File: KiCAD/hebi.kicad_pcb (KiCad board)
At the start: 4 copper layers, 49 x 49 mm, 99 parts, among them K1 CONN_3, K2 CONN_3, K3 CONN_3, K4 CONN_3, K5 CONN_3, P1 CONN_4, P2 CONN_4, P3 CONN_4, P4 CONN_4, P6 CONN_2, Q1 MOS_N_DIODE, Q10 MOS_N_DIODE, Q2 MOS_N_DIODE, Q3 MOS_N_DIODE, Q4 MOS_N_DIODE, Q5 MOS_N_DIODE, Q6 MOS_N_DIODE, Q7 MOS_N_DIODE, Q9 MOS_N_DIODE, SW1 SW_PUSH, SW2 SW_PUSH, SW3 SW_PUSH, U3 MCP1825S, U4 STM32F407VG, U5 XBEE, X1 8MHz

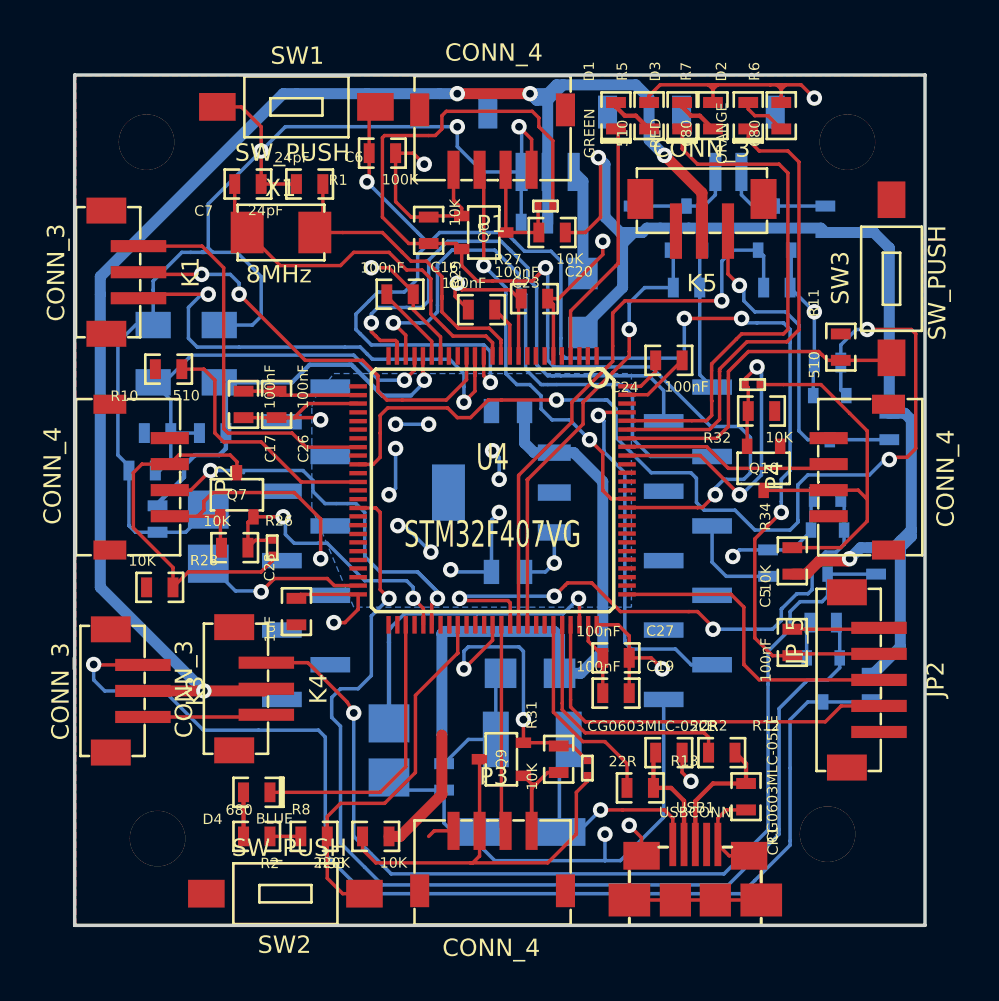
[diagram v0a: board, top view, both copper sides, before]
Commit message: Routed things, power planes added, rounded corners.
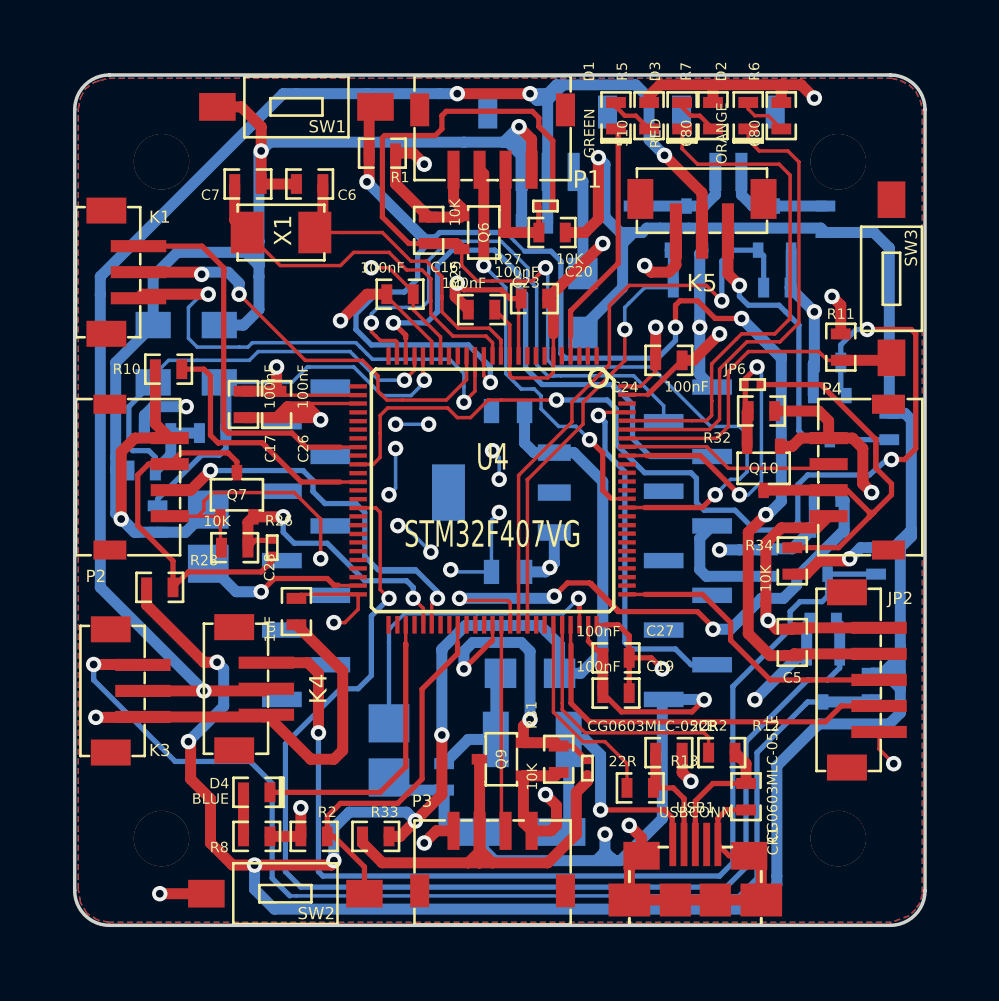
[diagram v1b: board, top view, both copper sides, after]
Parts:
- moved Taladro3mm 1.42 mm to (178.8, 116.7)
- moved Taladro3mm 1.25 mm to (217.8, 116.7)
- moved Taladro3mm 0.67 mm to (217.8, 155.7)
- moved Taladro3mm 0.22 mm to (178.8, 155.7)
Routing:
- net GND: track 218.7 -> 531.4 mm, vias 18 -> 28
- net VCC: track 110.9 -> 338.9 mm, vias 10 -> 18
- net +5V: track 116.3 -> 208.6 mm, vias 2 -> 8
- net /SERVO3_3V: track 58.1 -> 95.7 mm
- net /RESET: track 85.2 -> 122.8 mm
- net /XBEE_RX: track 33.3 -> 62.8 mm
- net /SERVO1_3V: track 64.7 -> 91.6 mm
- net /SERVO1_5V: track 66.5 -> 90.5 mm
- net /ADC3: track 22.9 -> 43.0 mm
- net /TX1_3V: track 61.9 -> 81.6 mm
- net /RX3: track 24.7 -> 43.9 mm
- net /TX3: track 21.4 -> 36.0 mm
- net /SERVO2_5V: track 59.0 -> 72.9 mm
- net /TX2: track 24.0 -> 37.8 mm
- net /LED1: track 14.3 -> 25.9 mm
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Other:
- outline, holes or cut-outs redrawn
- net class Medium added: clearance 0.254, trace_width 0.3048, via_dia 0.889, via_drill 0.635

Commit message: Fixed silkscreen (now it is nice)
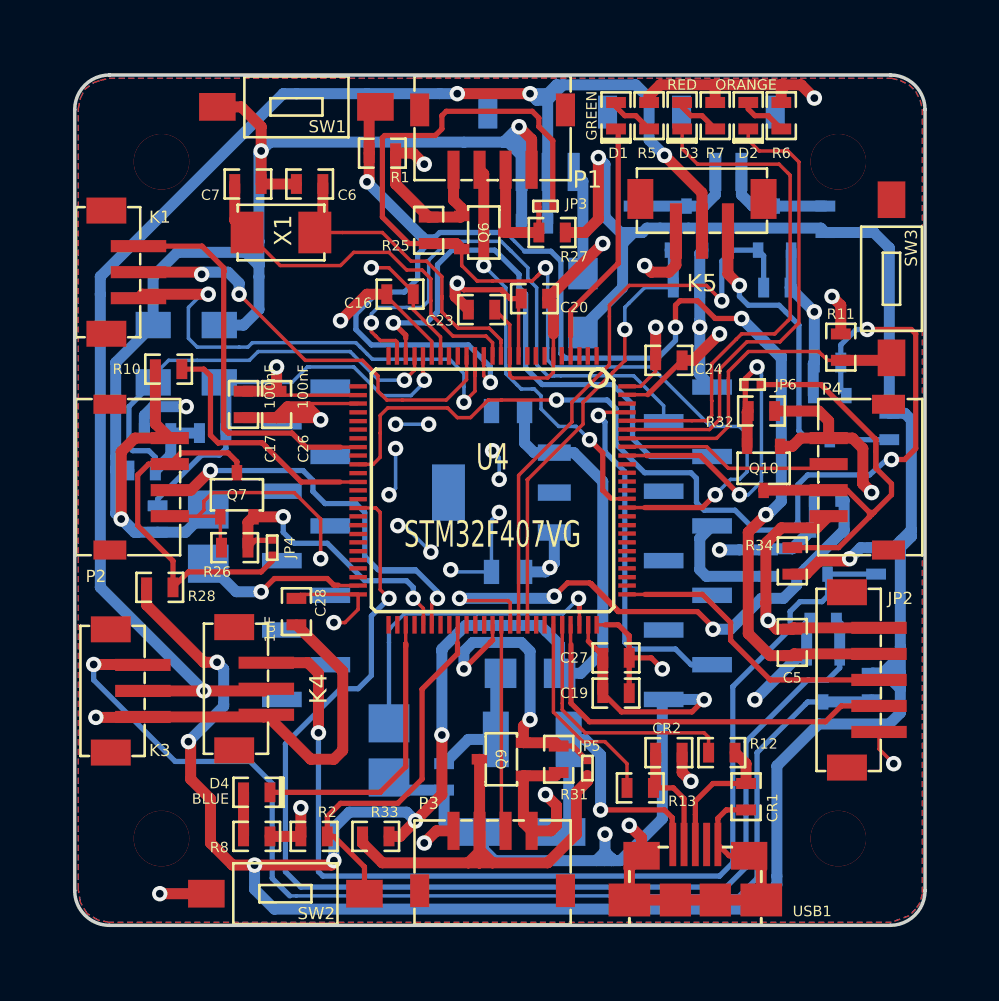
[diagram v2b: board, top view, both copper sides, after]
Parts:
- added G***: OSHW-logo, OSHW-logo, B.Cu at (186.6, 119.9)
- added G***: OSHW-logo, OSHW-logo, B.Cu at (209.3, 151.9)
- CR1, CR2: value CG0603MLC-05LE -> (none)
- moved R7 0.13 mm to (210.7, 114.0)
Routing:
- net N-00000101: track 2.56 -> 4.29 mm
- net N-00000102: track 2.76 -> 4.44 mm
- net N-00000103: track 2.69 -> 4.29 mm
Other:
- board text added: "Author: David Estevez Fernandez"
- board text added: "HEBI board STM32F4"
- board text added: "v0.1"

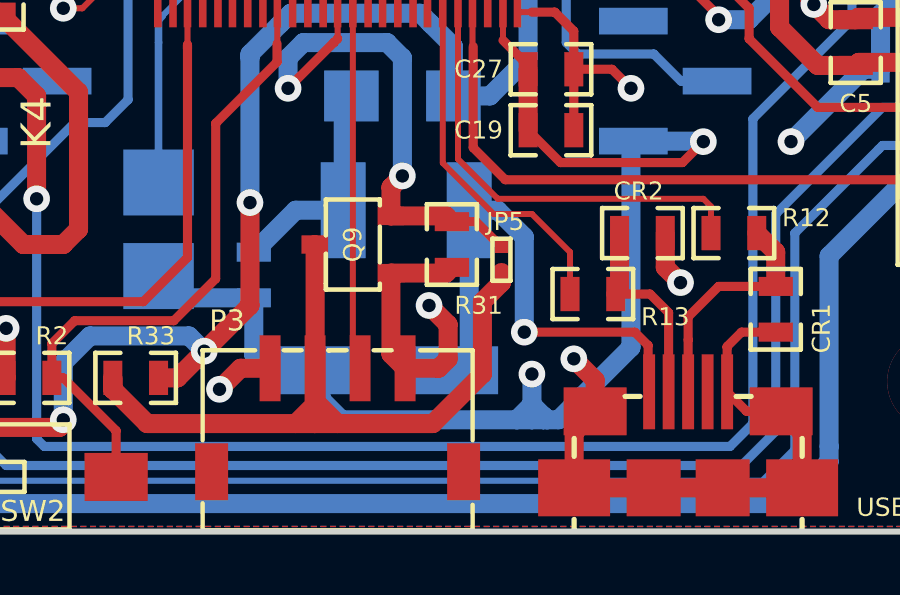
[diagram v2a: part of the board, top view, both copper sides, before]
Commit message: Modified electrolytic capacitor to tantalum one.
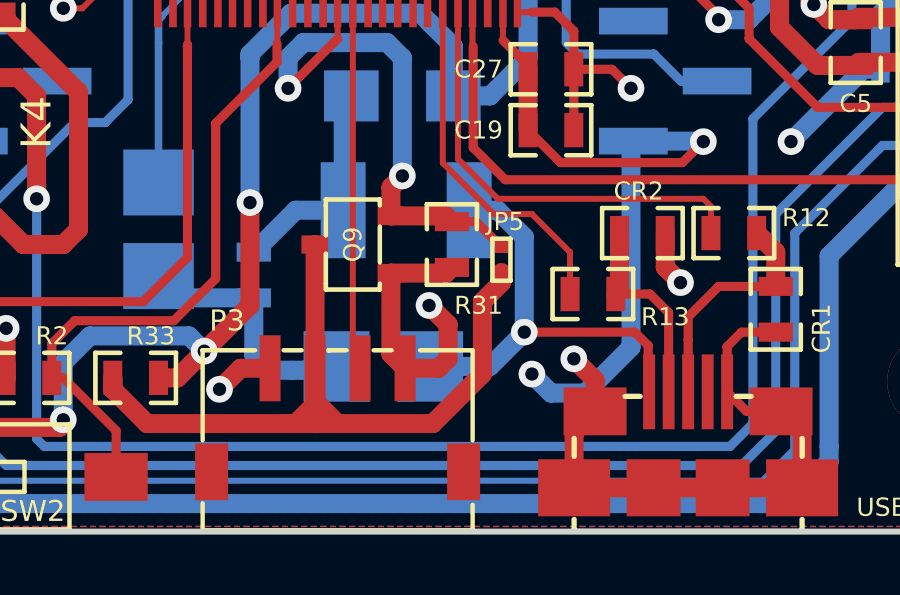
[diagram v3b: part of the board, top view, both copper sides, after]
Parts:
- C25: footprint c_elec_5x5.3 -> 1411_hebi
- CR1, CR2: value (none) -> CG0603MLC-05LE
- moved C25 0.18 mm to (199.4, 155.2), turned to 180 degrees
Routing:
- net GND: track 531.6 -> 518.7 mm
- net /VBUS: track 21.6 -> 19.3 mm
